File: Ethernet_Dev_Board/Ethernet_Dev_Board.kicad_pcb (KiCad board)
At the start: 4 copper layers, 79.9 x 65.2 mm, 115 parts, among them J101 Power In, J401 TAG-CONNECT_NL_10-POS_LEGS, Q201 PMV48XPA2R, U101 AZ1117, U102 74AUP1T08GWH, U103 1.2V, U201 WIZNET_W5500, U402 ESP32-WROOM-32E, U403 74LVC1G11W6, Y201 25MHz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

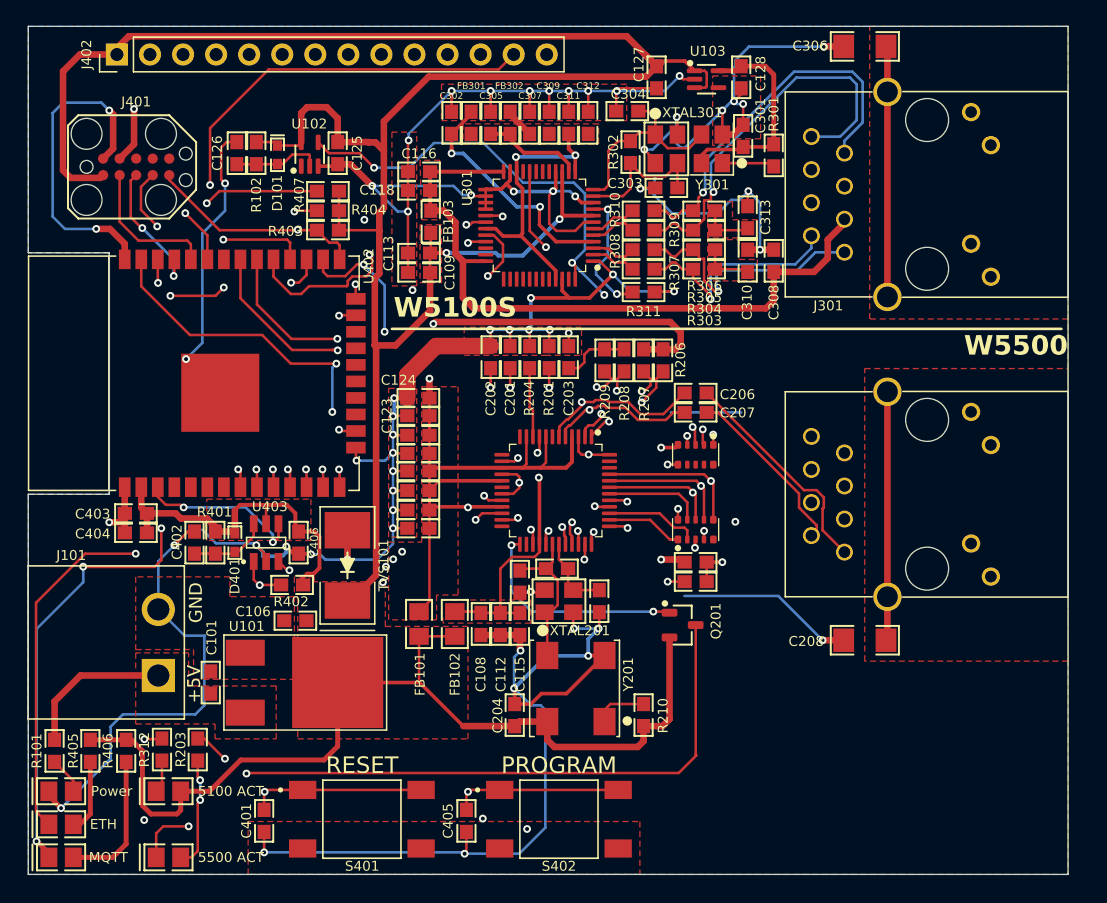
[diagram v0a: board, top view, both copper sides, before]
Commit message: Fixed DRC errors. Edited layout stack
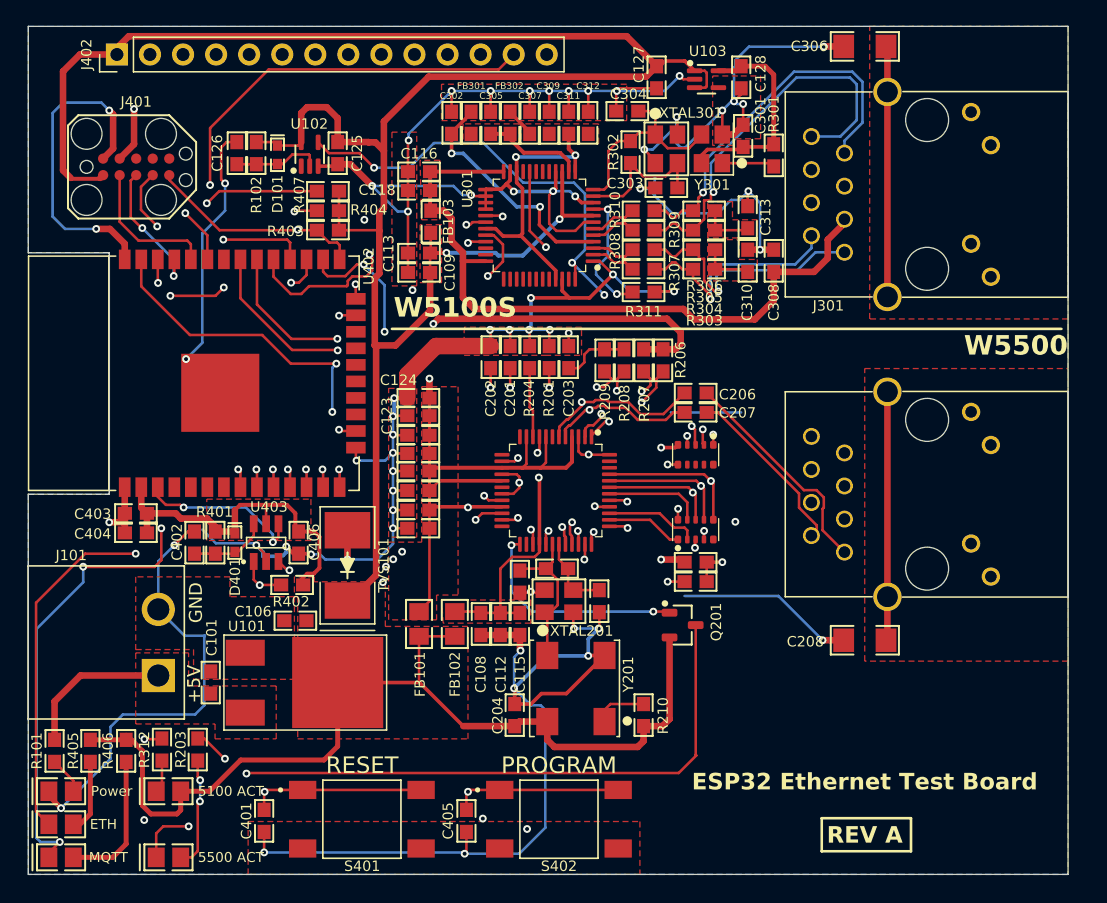
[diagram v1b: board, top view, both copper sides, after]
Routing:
- net +3.3V: track 279.3 -> 278.1 mm
- net Net-(U201C-ACTLED): track 55.0 -> 55.7 mm
- net +3.3VA2: track 53.5 -> 54.2 mm
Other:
- board text added: "ESP32 Ethernet Test Board REV A"

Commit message: Rev A Design files finish
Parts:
- moved C107 0.35 mm to (108.0, 84.2)
- moved C111 0.25 mm to (108.0, 82.8)
- moved C114 0.25 mm to (108.0, 81.2)
- moved C117 0.25 mm to (108.0, 79.8)
- moved C201 0.25 mm to (115.0, 71.0)
- moved C202 0.25 mm to (113.5, 71.0)
- moved C203 0.25 mm to (119.5, 71.0)
- moved R201 0.25 mm to (118.0, 71.0)
- moved R204 0.25 mm to (116.5, 71.0)
- moved C124 0.15 mm to (108.0, 73.8)
- moved C119 0.10 mm to (108.0, 78.2)
- moved R101 0.10 mm to (80.0, 100.9)
- moved R405 0.10 mm to (82.8, 100.9)
- moved R406 0.10 mm to (85.5, 100.9)
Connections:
- J402 pad 13: IO21 -> GND1
- U402 pad 33: IO21 -> ETH_RST
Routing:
- net IO21: track 37.4 -> 0.00 mm, vias 2 -> 0
- net +3.3V: track 278.1 -> 249.5 mm
- net ETH_RST: track 0.00 -> 15.2 mm, vias 0 -> 2
- net +3.3VA: track 107.0 -> 104.9 mm
- net Net-(Q201-G): track 17.1 -> 19.1 mm, vias 2 -> 3
- net SS: track 75.5 -> 73.7 mm
- net +1.2VA: track 19.9 -> 18.5 mm
- net ETH_EN: track 66.4 -> 66.5 mm, vias 5 -> 4
- net GND1: vias 68 -> 89
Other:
- board text added: "ETH EN"
- board text added: "MISO"
- board text added: "MOSI"
- board text added: "SCK"
- board text added: "SS"

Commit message: Added RG logo
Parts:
- added G***: LOGO, RG_Logo:Logo_1, F.Cu at (142.2, 100.3)

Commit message: Adjusted RG logo
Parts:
- moved G*** 0.25 mm to (142.2, 100.1)
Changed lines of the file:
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@@
 	(footprint "RG_Logo:Logo_1"
 		(layer "F.Cu")
-		(at 142.24 100.33)
+		(at 142.24 100.084424)
 		(property "Reference" "G***"
 			(at 0 0 0)
